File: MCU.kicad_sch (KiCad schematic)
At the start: 35 parts, among them J1 GT-USB-7010I, SW1 BOOT0, SW6 Reset, U1 STM32F722RETx, U2 AMS1117-3.3, X1 32.768kHz 7pF, Y1 16MHz 10pF

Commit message: 1. Update README with info on my KiCAD component library. 2. Add Fiducial markers. 3. Add LCSC IDs for all parts in BOM.
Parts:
- C12: LCSC (none) -> C25804
- C16, C17: LCSC (none) -> C1569
- D10, D8, D9: DPFNOTES (none) -> 5.8V Bidirectional 5V SOD-923 ESD and Surge Protection (TVS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; LCSC (none) -> C111566
- SW6: LCSC (none) -> C318884
- U1: DPFNOTES (none) -> 512KB 1.7V~3.6V 256KB 216MHz FLASH 50 LQFP-64(10x10) Microc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; LCSC (none) -> C118207
- X1: LCSC (none) -> C48615
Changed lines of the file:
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@@
 			)
 		)
+		(property "DPFNOTES" "512KB 1.7V~3.6V 256KB 216MHz FLASH 50 LQFP-64(10x10) Microcontrollers (MCU/MPU/SOC) ROHS STM32F722RET6"
+			(at 135.89 100.33 0)
+			(effects
+				(font
+					(size 1.27 1.27)
+				)
+				(hide yes)
+			)
+		)
+		(property "LCSC" "C118207"
+			(at 135.89 100.33 0)
+			(effects
+				(font
+					(size 1.27 1.27)
+				)
+				(hide yes)
+			)
+		)
 		(pin "19"
 		)
@@
 			)
 		)
-		(property "LCSC" ""
+		(property "LCSC" "C111566"
 			(at 182.88 104.14 0)
 			(effects
@@
 			)
 		)
-		(property "DPFNOTES" ""
+		(property "DPFNOTES" "5.8V Bidirectional 5V SOD-923 ESD and Surge Protection (TVS/ESD) ROHS - Some possibilities: C96512, C111566"
 			(at 182.88 104.14 0)
 			(effects
@@
 			)
 		)
-		(property "Datasheet" "~"
+		(property "Datasheet" "https://www.lcsc.com/datasheet/lcsc_datasheet_1808041445_ALPSALPINE-SSSS811101_C109335.pdf"
 			(at 71.12 62.23 0)
 			(effects
@@
 			)
 		)
-		(property "LCSC" ""
+		(property "LCSC" "C111566"
 			(at 187.96 104.14 0)
 			(effects
@@
 			)
 		)
-		(property "DPFNOTES" ""
+		(property "DPFNOTES" "5.8V Bidirectional 5V SOD-923 ESD and Surge Protection (TVS/ESD) ROHS - Some possibilities: C96512, C111566"
 			(at 187.96 104.14 0)
 			(effects
@@
 			)
 		)
-		(property "Datasheet" "~"
+		(property "Datasheet" "https://www.lcsc.com/datasheet/lcsc_datasheet_2304140030_FH--Guangdong-Fenghua-Advanced-Tech-0402CG4R7C500NT_C1569.pdf"
 			(at 82.55 119.38 0)
 			(effects
@@
 			)
 		)
-		(property "LCSC" ""
+		(property "LCSC" "C1569"
 			(at 82.55 119.38 0)
 			(effects
@@
 			)
 		)
+		(property "LCSC" "C318884"
+			(at 36.83 59.69 0)
+			(effects
+				(font
+					(size 1.27 1.27)
+				)
+				(hide yes)
+			)
+		)
 		(pin "1"
 		)
@@
 			)
 		)
-		(property "Datasheet" "~"
+		(property "Datasheet" "https://www.lcsc.com/datasheet/lcsc_datasheet_2304140030_FH--Guangdong-Fenghua-Advanced-Tech-0402CG4R7C500NT_C1569.pdf"
 			(at 67.31 119.38 0)
 			(effects
@@
 			)
 		)
-		(property "LCSC" ""
+		(property "LCSC" "C1569"
 			(at 67.31 119.38 0)
 			(effects
@@
 			)
 		)
-		(property "Datasheet" "~"
+		(property "Datasheet" "https://www.lcsc.com/datasheet/lcsc_datasheet_2206010100_UNI-ROYAL-Uniroyal-Elec-0402WGF1002TCE_C25744.pdf"
 			(at 85.09 66.04 0)
 			(effects
@@
 			)
 		)
-		(property "LCSC" ""
+		(property "LCSC" "C48615"
 			(at 74.93 115.57 0)
 			(effects
@@
 			)
 		)
-		(property "LCSC" ""
+		(property "LCSC" "C111566"
 			(at 195.58 104.14 0)
 			(effects
@@
 			)
 		)
-		(property "DPFNOTES" ""
+		(property "DPFNOTES" "5.8V Bidirectional 5V SOD-923 ESD and Surge Protection (TVS/ESD) ROHS - Some possibilities: C96512, C111566"
 			(at 195.58 104.14 0)
 			(effects
@@
 			)
 		)
-		(property "Datasheet" "~"
+		(property "Datasheet" "https://www.lcsc.com/datasheet/lcsc_datasheet_2206010045_UNI-ROYAL-Uniroyal-Elec-0603WAF1002T5E_C25804.pdf"
 			(at 109.22 127 0)
 			(effects
@@
 			)
 		)
-		(property "LCSC" ""
+		(property "LCSC" "C25804"
 			(at 109.22 127 0)
 			(effects

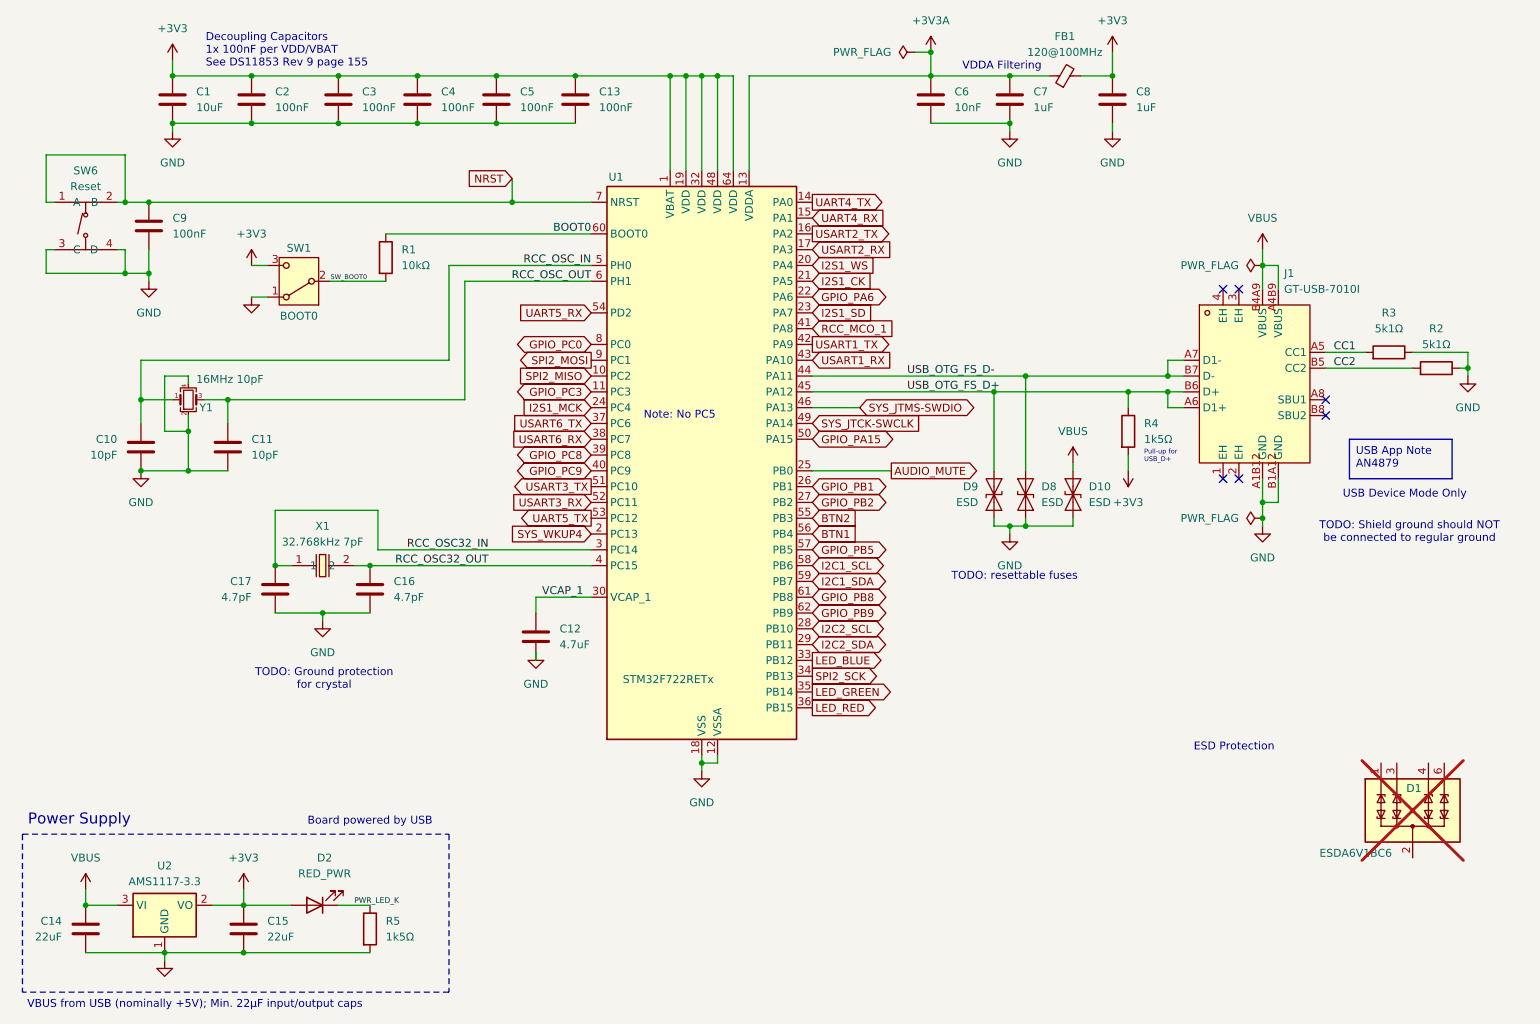
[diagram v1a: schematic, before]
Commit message: 1. Remove unused components on schematic. 2. Find other color LEDs in JLCPCB.
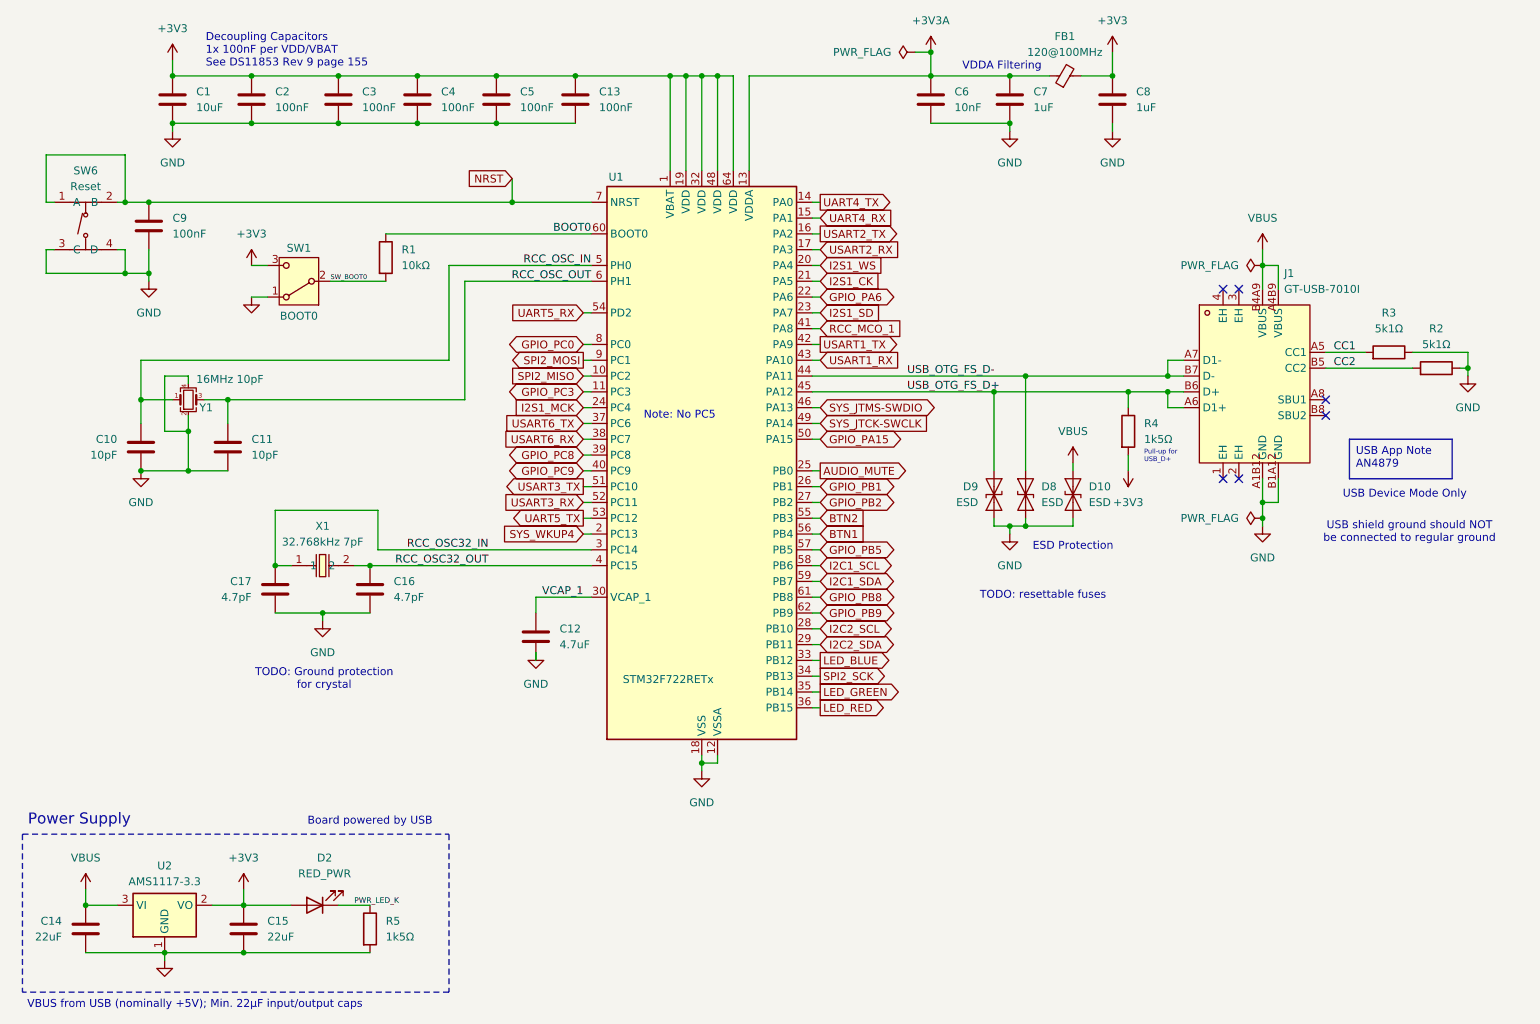
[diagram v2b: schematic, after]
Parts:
- removed D1: ESDA6V1BC6, Package_TO_SOT_SMD:SOT-23-6, symbol Power_Protection:ESDA6V1BC6
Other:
- note added: "USB shield ground should NOT be connected to regular ground"
- note removed: "TODO: Shield ground should NOT be connected to regular ground"

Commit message: Reviewing every item in the BOM against LCSC database. Found several errors already. Part way done.
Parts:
- C1, C6: JLC Basic Part (none) -> Basic
- C10, C11: DPFNOTES (none) -> 50V 10pF C0G ±5% 0402 Multilayer Ceramic Capacitors MLCC - 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; JLC Basic Part (none) -> Basic
- C12: DPFNOTES ESR between 0.1 and 0.2 ohms per DS11853 Rev 9 page 105 -> NEEDED: ESR between 0.1 and 0.2 ohms per DS11853 Rev 9 page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; JLC Basic Part (none) -> Basic; LCSC C25804 -> C19666; Manu Part (none) -> CL10A475KO8NNNC
- C13, C2, C3, C4, C5, C9: DPFNOTES (none) -> 50V 100nF X7R ±10% 0402 Multilayer Ceramic Capacitors MLCC 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; JLC Basic Part (none) -> Basic
- C14, C15: DPFNOTES (none) -> 25V 22uF X5R ±20% 0805 Multilayer Ceramic Capacitors MLCC -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; JLC Basic Part (none) -> Basic; Manu Part (none) -> CL21A226MAQNNNE
- C16, C17: DPFNOTES 7pF crystal, 3-5pF Cs, 7 - 3 = 4 x 2 = 8 -> 7 - 5 = 2 x 2 = 4 -> 7pF crystal, 3-5pF Cs, 7 - 3 = 4 x 2 = 8 -> 7 - 5 = 2 x 2 = 4 --- 50V 4.7pF C0G 0402 Multilayer Ceramic Capacitors MLCC - SMD/SMT ROHS; JLC Basic Part (none) -> Extended; Manu Part (none) -> 0402CG4R7C500NT
- C7, C8: DPFNOTES (none) -> 25V 1uF X5R ±10% 0402 Multilayer Ceramic Capacitors MLCC - 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; JLC Basic Part (none) -> Basic
- D10, D8, D9: JLC Basic Part (none) -> Extended; Manu Part (none) -> ESD9B5.0ST5G; Manufacturer (none) -> onsemi
- D2: DPFNOTES Hubei KENTO Elec KT-0603R -> -40℃~+85℃ Red 0603 LED Indication - Discrete ROHS; JLC Basic Part (none) -> Basic; Manu Part (none) -> KT-0603R; Manufacturer (none) -> Hubei KENTO Elec
- FB1: DPFNOTES TAI-TECH FCM1608KF-601T05, used on Nucleo-F767ZI -> TAI-TECH FCM1608KF-601T05, used on Nucleo-F767ZI --- 500mΩ 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; JLC Basic Part (none) -> Extended; Manu Part (none) -> FCM1608KF-601T05; Manufacturer (none) -> TAI-TECH
- J1: DPFNOTES (none) -> Female Type-C USB Connectors ROHS; JLC Basic Part (none) -> Extended; Manu Part (none) -> GT-USB-7010i; Manufacturer (none) -> G-Switch
- R1: JLC Basic Part (none) -> Basic; Manu Part (none) -> 0402WGF1002TCE; Manufacturer (none) -> UNI-ROYAL(Uniroyal Elec)
- R2, R3: DPFNOTES (none) -> 62.5mW Thick Film Resistors 50V ±100ppm/℃ ±1% 5.1kΩ 0402 Ch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; JLC Basic Part (none) -> Basic; Manu Part (none) -> 0402WGF5101TCE; Manufacturer (none) -> UNI-ROYAL(Uniroyal Elec)
- R4, R5: DPFNOTES (none) -> 62.5mW Thick Film Resistors 50V ±100ppm/℃ ±1% 1.5kΩ 0402 Ch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; JLC Basic Part (none) -> Basic; Manu Part (none) -> 0402WGF1501TCE; Manufacturer (none) -> UNI-ROYAL(Uniroyal Elec)

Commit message: Finished checking all parts against LCSC IDs. Found remaining errors. Added manufacturer part numbers to all parts.
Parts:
- C1: Manu Part (none) -> CL10A106MA8NRNC; Manufacturer (none) -> Samsung Electro-Mechanics
- C10, C11: Manu Part (none) -> CL05C100JB5NNNC; Manufacturer (none) -> Samsung Electro-Mechanics
- C12, C14, C15: Manufacturer (none) -> Samsung Electro-Mechanics
- C13, C2, C3, C4, C5, C9: Manu Part (none) -> CL05B104KB54PNC; Manufacturer (none) -> Samsung Electro-Mechanics
- C16, C17: Manufacturer (none) -> FH (Guangdong Fenghua Advanced Tech)
- C6: Manu Part (none) -> CL05B103KB5NNNC; Manufacturer (none) -> Samsung Electro-Mechanics
- C7, C8: Manu Part (none) -> CL05A105KA5NQNC; Manufacturer (none) -> Samsung Electro-Mechanics
- SW1: DPFNOTES ALPSALPINE SSSS811101, Like C&K PCM-12-SMT PCM12SMTR -> ALPSALPINE SSSS811101, Like C&K PCM-12-SMT PCM12SMTR --- 30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; JLC Basic Part (none) -> Extended; Manu Part (none) -> SSSS811101; Manufacturer (none) -> ALPSALPINE
- SW6: DPFNOTES (none) -> None Without 50mA 5.1mm 100000 Times 160gf 12V 5.1mm 1.5mm 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; JLC Basic Part (none) -> Basic; Manu Part (none) -> TS-1187A-B-A-B; Manufacturer (none) -> XKB Connection
- U1: JLC Basic Part (none) -> Extended; Manu Part (none) -> STM32F722RET6; Manufacturer (none) -> STMicroelectronics
- U2: DPFNOTES (none) -> 72dB@(120Hz) 1A Fixed 3.3V Positive electrode SOT-223 Volta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; JLC Basic Part (none) -> Basic; Manu Part (none) -> AMS1117-3.3; Manufacturer (none) -> Advanced Monolithic Systems
- X1: JLC Basic Part (none) -> Extended; Manu Part (none) -> Q13FC13500002; Manufacturer (none) -> Seiko Epson
- Y1: DPFNOTES YXC Crystal Oscillators X322516MMB4SI -> 16MHz Surface Mount Crystal 10pF ±10ppm ±20ppm SMD3225-4P C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; JLC Basic Part (none) -> Extended; Manu Part (none) -> X322516MMB4SI; Manufacturer (none) -> YXC Crystal Oscillators
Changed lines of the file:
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@@
 			)
 		)
-		(property "Manu Part" ""
+		(property "Manu Part" "STM32F722RET6"
 			(at 135.89 100.33 0)
 			(effects
@@
 			)
 		)
-		(property "Manufacturer" ""
+		(property "Manufacturer" "STMicroelectronics"
 			(at 135.89 100.33 0)
 			(effects
@@
 			)
 		)
+		(property "JLC Basic Part" "Extended"
+			(at 135.89 100.33 0)
+			(effects
+				(font
+					(size 1.27 1.27)
+				)
+				(hide yes)
+			)
+		)
 		(pin "19"
 		)
@@
 			)
 		)
-		(property "Manu Part" ""
+		(property "Manu Part" "CL05B104KB54PNC"
 			(at 115.57 40.64 0)
 			(effects
@@
 			)
 		)
-		(property "Manufacturer" ""
+		(property "Manufacturer" "Samsung Electro-Mechanics"
 			(at 115.57 40.64 0)
 			(effects
@@
 			)
 		)
-		(property "Manu Part" ""
+		(property "Manu Part" "CL05B104KB54PNC"
 			(at 63.5 40.64 0)
 			(effects
@@
 			)
 		)
-		(property "Manufacturer" ""
+		(property "Manufacturer" "Samsung Electro-Mechanics"
 			(at 63.5 40.64 0)
 			(effects
@@
 			)
 		)
-		(property "DPFNOTES" "ALPSALPINE SSSS811101, Like C&K PCM-12-SMT PCM12SMTR"
+		(property "DPFNOTES" "ALPSALPINE SSSS811101, Like C&K PCM-12-SMT PCM12SMTR --- 300mA Horizontal attachment Single Pole Double Throw (SPDT) 5V 10,000 times SMD Slide Switches ROHS"
 			(at 71.12 69.85 0)
 			(effects
@@
 			)
 		)
-		(property "Manu Part" ""
+		(property "Manu Part" "SSSS811101"
 			(at 71.12 69.85 0)
 			(effects
@@
 			)
 		)
-		(property "Manufacturer" ""
+		(property "Manufacturer" "ALPSALPINE"
 			(at 71.12 69.85 0)
 			(effects
@@
 			)
 		)
+		(property "JLC Basic Part" "Extended"
+			(at 71.12 69.85 0)
+			(effects
+				(font
+					(size 1.27 1.27)
+				)
+				(hide yes)
+			)
+		)
 		(pin "3"
 		)
@@
 			)
 		)
-		(property "Manu Part" ""
+		(property "Manu Part" "CL05C100JB5NNNC"
 			(at 59.69 96.52 0)
 			(effects
@@
 			)
 		)
-		(property "Manufacturer" ""
+		(property "Manufacturer" "Samsung Electro-Mechanics"
 			(at 59.69 96.52 0)
 			(effects
@@
 			)
 		)
-		(property "Manu Part" ""
+		(property "Manu Part" "CL05B103KB5NNNC"
 			(at 172.72 40.64 0)
 			(effects
@@
 			)
 		)
-		(property "Manufacturer" ""
+		(property "Manufacturer" "Samsung Electro-Mechanics"
 			(at 172.72 40.64 0)
 			(effects
@@
 			)
 		)
-		(property "Manu Part" ""
+		(property "Manu Part" "CL05B104KB54PNC"
 			(at 77.47 40.64 0)
 			(effects
@@
 			)
 		)
-		(property "Manufacturer" ""
+		(property "Manufacturer" "Samsung Electro-Mechanics"
 			(at 77.47 40.64 0)
 			(effects
@@
 			)
 		)
-		(property "Manufacturer" ""
+		(property "Manufacturer" "FH (Guangdong Fenghua Advanced Tech)"
 			(at 82.55 119.38 0)
 			(effects
@@
 			)
 		)
-		(property "Manu Part" ""
+		(property "Manu Part" "TS-1187A-B-A-B"
 			(at 36.83 59.69 0)
 			(effects
@@
 			)
 		)
-		(property "Manufacturer" ""
+		(property "Manufacturer" "XKB Connection"
 			(at 36.83 59.69 0)
 			(effects
@@
 			)
 		)
+		(property "DPFNOTES" "None Without 50mA 5.1mm 100000 Times 160gf 12V 5.1mm 1.5mm Round Button Standing paste SPST SMD Tactile Switches ROHS"
+			(at 36.83 59.69 0)
+			(effects
+				(font
+					(size 1.27 1.27)
+				)
+				(hide yes)
+			)
+		)
+		(property "JLC Basic Part" "Basic"
+			(at 36.83 59.69 0)
+			(effects
+				(font
+					(size 1.27 1.27)
+				)
+				(hide yes)
+			)
+		)
 		(pin "1"
 		)
@@
 			)
 		)
-		(property "Manufacturer" ""
+		(property "Manufacturer" "FH (Guangdong Fenghua Advanced Tech)"
 			(at 67.31 119.38 0)
 			(effects
@@
 			)
 		)
-		(property "Manu Part" ""
+		(property "Manu Part" "CL05C100JB5NNNC"
 			(at 45.72 96.52 0)
 			(effects
@@
 			)
 		)
-		(property "Manufacturer" ""
+		(property "Manufacturer" "Samsung Electro-Mechanics"
 			(at 45.72 96.52 0)
 			(effects
@@
 			)
 		)
-		(property "Manu Part" ""
+		(property "Manu Part" "CL05B104KB54PNC"
 			(at 102.87 40.64 0)
 			(effects
@@
 			)
 		)
-		(property "Manufacturer" ""
+		(property "Manufacturer" "Samsung Electro-Mechanics"
 			(at 102.87 40.64 0)
 			(effects
@@
 			)
 		)
-		(property "Manu Part" ""
+		(property "Manu Part" "CL05A105KA5NQNC"
 			(at 185.42 40.64 0)
 			(effects
@@
 			)
 		)
-		(property "Manufacturer" ""
+		(property "Manufacturer" "Samsung Electro-Mechanics"
 			(at 185.42 40.64 0)
 			(effects
@@
 			)
 		)
-		(property "Manu Part" ""
+		(property "Manu Part" "CL05B104KB54PNC"
 			(at 46.99 60.96 0)
 			(effects
@@
 			)
 		)
-		(property "Manufacturer" ""
+		(property "Manufacturer" "Samsung Electro-Mechanics"
 			(at 46.99 60.96 0)
 			(effects
@@
 			)
 		)
-		(property "Manufacturer" ""
+		(property "Manufacturer" "Samsung Electro-Mechanics"
 			(at 62.23 173.99 0)
 			(effects
@@
 			)
 		)
-		(property "Manu Part" ""
+		(property "Manu Part" "Q13FC13500002"
 			(at 74.93 115.57 0)
 			(effects
@@
 			)
 		)
-		(property "Manufacturer" ""
+		(property "Manufacturer" "Seiko Epson"
 			(at 74.93 115.57 0)
 			(effects
@@
 			)
 		)
+		(property "JLC Basic Part" "Extended"
+			(at 74.93 115.57 0)
+			(effects
+				(font
+					(size 1.27 1.27)
+				)
+				(hide yes)
+			)
+		)
 		(pin "2"
 		)
@@
 			)
 		)
-		(property "Manu Part" ""
+		(property "Manu Part" "CL05B104KB54PNC"
 			(at 90.17 40.64 0)
 			(effects
@@
 			)
 		)
-		(property "Manufacturer" ""
+		(property "Manufacturer" "Samsung Electro-Mechanics"
 			(at 90.17 40.64 0)
 			(effects
@@
 			)
 		)
-		(property "Manufacturer" ""
+		(property "Manufacturer" "Samsung Electro-Mechanics"
 			(at 36.83 173.99 0)
 			(effects
@@
 			)
 		)
-		(property "Datasheet" "~"
+		(property "Datasheet" "https://www.lcsc.com/datasheet/lcsc_datasheet_2403291504_YXC-Crystal-Oscillators-X322516MMB4SI_C112972.pdf"
 			(at 53.34 88.9 0)
 			(effects
@@
 			)
 		)
-		(property "DPFNOTES" "YXC Crystal Oscillators X322516MMB4SI"
+		(property "DPFNOTES" "16MHz Surface Mount Crystal 10pF ±10ppm ±20ppm SMD3225-4P Crystals ROHS"
 			(at 53.34 88.9 0)
 			(effects
@@
 			)
 		)
-		(property "Manu Part" ""
+		(property "Manu Part" "X322516MMB4SI"
 			(at 53.34 88.9 0)
 			(effects
@@
 			)
 		)
-		(property "Manufacturer" ""
+		(property "Manufacturer" "YXC Crystal Oscillators"
 			(at 53.34 88.9 0)
 			(effects
@@
 			)
 		)
+		(property "JLC Basic Part" "Extended"
+			(at 53.34 88.9 0)
+			(effects
+				(font
+					(size 1.27 1.27)
+				)
+				(hide yes)
+			)
+		)
 		(pin "3"
 		)
@@
 			)
 		)
-		(property "Manu Part" ""
+		(property "Manu Part" "CL05A105KA5NQNC"
 			(at 201.93 40.64 0)
 			(effects
@@
 			)
 		)
-		(property "Manufacturer" ""
+		(property "Manufacturer" "Samsung Electro-Mechanics"
 			(at 201.93 40.64 0)
 			(effects
@@
 			)
 		)
-		(property "DPFNOTES" ""
+		(property "DPFNOTES" "72dB@(120Hz) 1A Fixed 3.3V Positive electrode SOT-223 Voltage Regulators - Linear, Low Drop Out (LDO) Regulators ROHS"
 			(at 49.53 170.18 0)
 			(effects
@@
 			)
 		)
-		(property "Manu Part" ""
+		(property "Manu Part" "AMS1117-3.3"
 			(at 49.53 170.18 0)
 			(effects
@@
 			)
 		)
-		(property "Manufacturer" ""
+		(property "Manufacturer" "Advanced Monolithic Systems"
 			(at 49.53 170.18 0)
 			(effects
@@
 			)
 		)
+		(property "JLC Basic Part" "Basic"
+			(at 49.53 170.18 0)
+			(effects
+				(font
+					(size 1.27 1.27)
+				)
+				(hide yes)
+			)
+		)
 		(pin "2"
 		)
@@
 			)
 		)
-		(property "Manufacturer" ""
+		(property "Manufacturer" "Samsung Electro-Mechanics"
 			(at 109.22 127 0)
 			(effects
@@
 			)
 		)
-		(property "Manu Part" ""
+		(property "Manu Part" "CL10A106MA8NRNC"
 			(at 50.8 40.64 0)
 			(effects
@@
 			)
 		)
-		(property "Manufacturer" ""
+		(property "Manufacturer" "Samsung Electro-Mechanics"
 			(at 50.8 40.64 0)
 			(effects
